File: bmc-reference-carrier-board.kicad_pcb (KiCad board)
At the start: 8 copper layers, 120.4 x 90 mm, 40 parts, among them J1 PCB-Edge_DC-SCM-2.1_2x84_Rev-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, J2 USB-C_GCT_USB4105-GF-A, J3 USB-C_GCT_USB4105-GF-A, J4 USB-C_GCT_USB4105-GF-A, J5 L834-1G1T-S7, J6 DisplayPort-Mini_TE_2129320-3, J7 Bus_M.2_1-2199230-6, J8 TFM-107-01-X-D-RE1-WT, Q1 BSS84AKW, U1 USB2514B-I_M2, U14 OSM-L_Carrier-side, U15 CBTL02043ABQ, U2 RTL8211FS-CG, U3 SDINBDG4-8G, U5 FT4232H_VQFN, U6 NCP718BSN330T1G, U7 AP22615A_TSOT26, U8 AP22615A_TSOT26, Y1 Resonator_12MHz_ABM8G

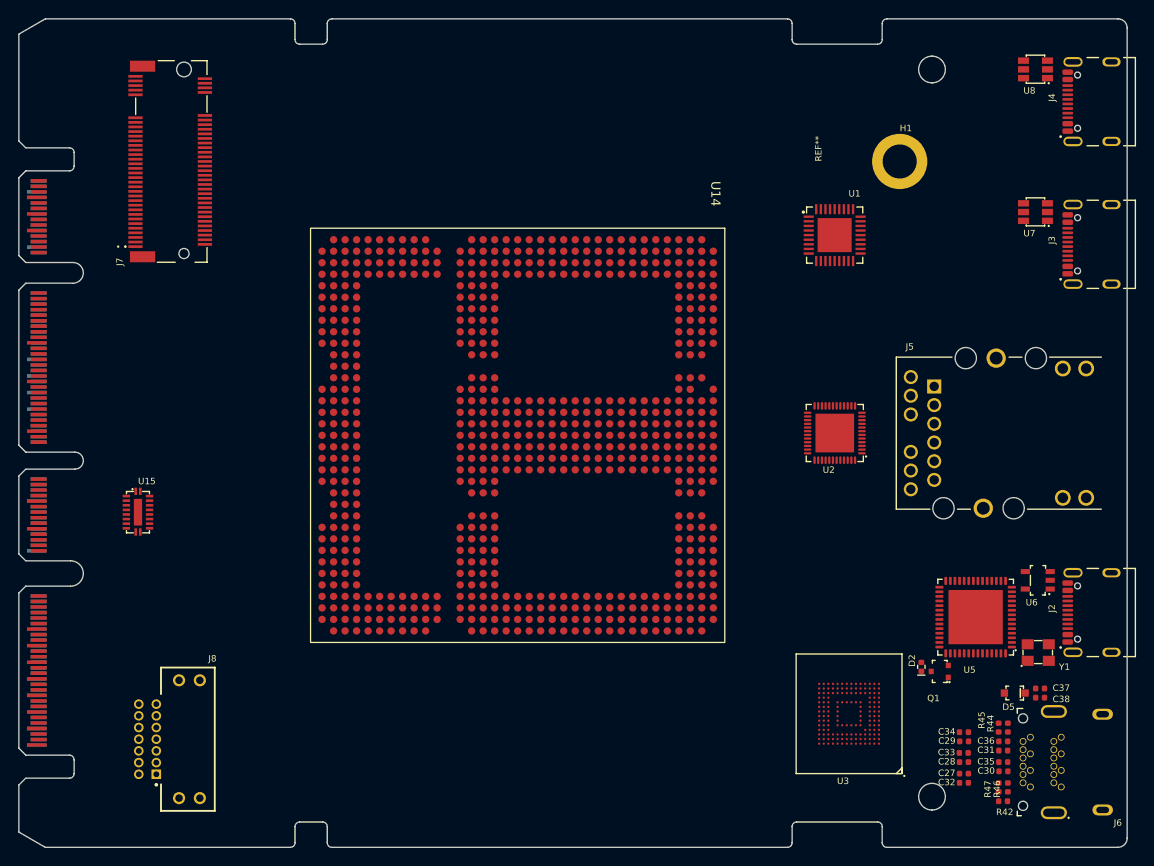
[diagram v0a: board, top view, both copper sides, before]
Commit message: [#82190] Update PCB from schematic
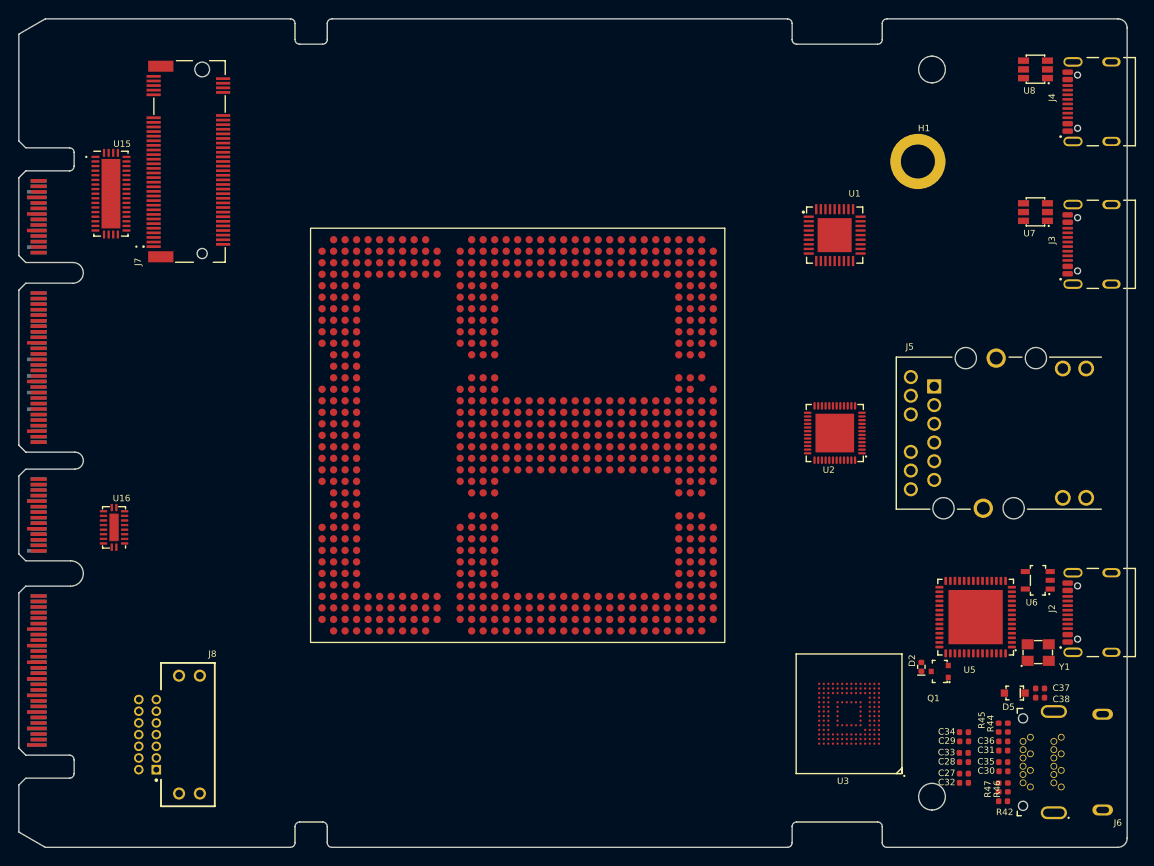
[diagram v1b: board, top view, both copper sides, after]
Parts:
- removed REF**: Mech_M2_2280_H2.5mm, antmicro-footprints:Mech_M2_2280_H2.5mm
- added U16: TMUXHS4212IRKSR, antmicro-footprints:VQFN-20_1EP_4.5x2.5mm_P0.5mm, F.Cu at (105.4, 96.2)
- U15: value CBTL02043ABQ -> TMUXHS4412RUAR; footprint antmicro-footprints:DHVQFN-20-1EP_2.5x4.5_P0.5mm -> antmicro-footprints:WQFN-42-1EP_3.5x9mm_P0.5mm
- moved U15 34.7 mm to (105.1, 60.0)
- moved H1 1.98 mm to (192.7, 56.5)
- moved J7 1.98 mm to (113.5, 56.5)
- moved J8 0.50 mm to (109.0, 118.8)
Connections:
- net /OSM L/OSM_PCIe_A.RX+ renamed /DC-SCM 2.1 connector/DC-SCM_PCIe0.RX2-
- net /OSM L/OSM_PCIe_A.RX- renamed /DC-SCM 2.1 connector/DC-SCM_PCIe0.RX2+
- net /OSM L/OSM_USB_C_SS.RX- renamed /PCIe - SGMII Mux/~{PCIE_USB_MUX_OE}
- net /OSM L/OSM_USB_C_SS.TX+ renamed /PCIe - SGMII Mux/PCIE_USB_MUX_SEL
- net /PCIe - USB Mux/PCIe/USB.RX+ renamed /DC-SCM 2.1 connector/DC-SCM_PCIe0.TX1+
- net /PCIe - USB Mux/PCIe/USB.RX- renamed /DC-SCM 2.1 connector/DC-SCM_PCIe0.TX1-
- net /PCIe - USB Mux/PCIe/USB.TX+ renamed /DC-SCM 2.1 connector/DC-SCM_PCIe0.RX1+
- net /PCIe - USB Mux/PCIe/USB.TX- renamed /DC-SCM 2.1 connector/DC-SCM_PCIe0.RX1-
- J7 pad 11: unconnected-(J7-PET3_N-Pad11) -> /DC-SCM 2.1 connector/DC-SCM_PCIe0.TX3-
- J7 pad 13: unconnected-(J7-PET3_P-Pad13) -> /DC-SCM 2.1 connector/DC-SCM_PCIe0.TX3+
- J7 pad 17: unconnected-(J7-PER2_N-Pad17) -> /PCIe - SGMII Mux/PCIE_x4.RX2-
- J7 pad 19: unconnected-(J7-PER2_P-Pad19) -> /PCIe - SGMII Mux/PCIE_x4.RX2+
- J7 pad 23: unconnected-(J7-PET2_N-Pad23) -> /PCIe - SGMII Mux/PCIE_x4.TX2-
- J7 pad 25: unconnected-(J7-PET2_P-Pad25) -> /PCIe - SGMII Mux/PCIE_x4.TX2+
- J7 pad 29: unconnected-(J7-PER1_N-Pad29) -> /PCIe - SGMII Mux/PCIE_x4.RX1-
- J7 pad 31: unconnected-(J7-PER1_P-Pad31) -> /PCIe - SGMII Mux/PCIE_x4.RX1+
- J7 pad 35: unconnected-(J7-PET1_N-Pad35) -> /PCIe - SGMII Mux/PCIE_x4.TX1-
- J7 pad 37: unconnected-(J7-PET1_P-Pad37) -> /PCIe - SGMII Mux/PCIE_x4.TX1+
- J7 pad 41: unconnected-(J7-PER0_N-Pad41) -> /DC-SCM 2.1 connector/DC-SCM_PCIe0.RX0-
- J7 pad 43: unconnected-(J7-PER0_P-Pad43) -> /DC-SCM 2.1 connector/DC-SCM_PCIe0.RX0+
- J7 pad 47: unconnected-(J7-PET0_N-Pad47) -> /DC-SCM 2.1 connector/DC-SCM_PCIe0.TX0-
- J7 pad 49: unconnected-(J7-PET0_P-Pad49) -> /DC-SCM 2.1 connector/DC-SCM_PCIe0.TX0+
- J7 pad 5: unconnected-(J7-PER3_N-Pad5) -> /DC-SCM 2.1 connector/DC-SCM_PCIe0.RX3-
- J7 pad 7: unconnected-(J7-PER3_P-Pad7) -> /DC-SCM 2.1 connector/DC-SCM_PCIe0.RX3+
- U15 pad 1: +3V3 -> unconnected-(U15-NC-Pad1)
- U15 pad 10: +3V3 -> /DC-SCM 2.1 connector/DC-SCM_PCIe0.TX2+
- U15 pad 11: GND -> /DC-SCM 2.1 connector/DC-SCM_PCIe0.TX2-
- U15 pad 12: /OSM L/OSM_PCIe_A.TX- -> unconnected-(U15-NC-Pad12)
- U15 pad 13: /OSM L/OSM_PCIe_A.TX+ -> /PCIe - SGMII Mux/VCC
- U15 pad 16: /OSM L/OSM_USB_C_SS.TX- -> GND
- U15 pad 19: /OSM L/OSM_USB_C_SS.RX+ -> unconnected-(U15-NC-Pad19)
- U15 pad 2: GND -> unconnected-(U15-NC-Pad2)
- U15 pad 20: GND -> unconnected-(U15-NC-Pad20)
- U15 pad 5: GND -> /PCIe - SGMII Mux/VCC
- U15 pad 6: +3V3 -> GND
- U15 pad 9: /PCIe - USB Mux/pcie_usb_mux_sel -> GND

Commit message: [#82190] Add logotype
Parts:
- added REF**: LOGO, antmicro-footprints:nxp_logo, F.Cu at (160.2, 47.6)
- added REF**: OSHW-Logo_5.7x6mm_Copper, antmicro-footprints:OSHW-Logo_5.7x6mm_Copper, F.Cu at (155.4, 125.7)
- added REF**: LOGO, antmicro-footprints:lattice_logo, F.Cu at (138.3, 48.3)
- added REF**: antmicro-logo_scaled_15mm, antmicro-footprints:antmicro-logo_scaled_15mm, F.Cu at (169.0, 125.9)
- added REF**: OSHW-Logo_5.7x6mm_Mask, antmicro-footprints:OSHW-Logo_5.7x6mm_Mask, F.Cu at (155.4, 125.7)
- moved U3 5.42 mm to (183.2, 111.5)

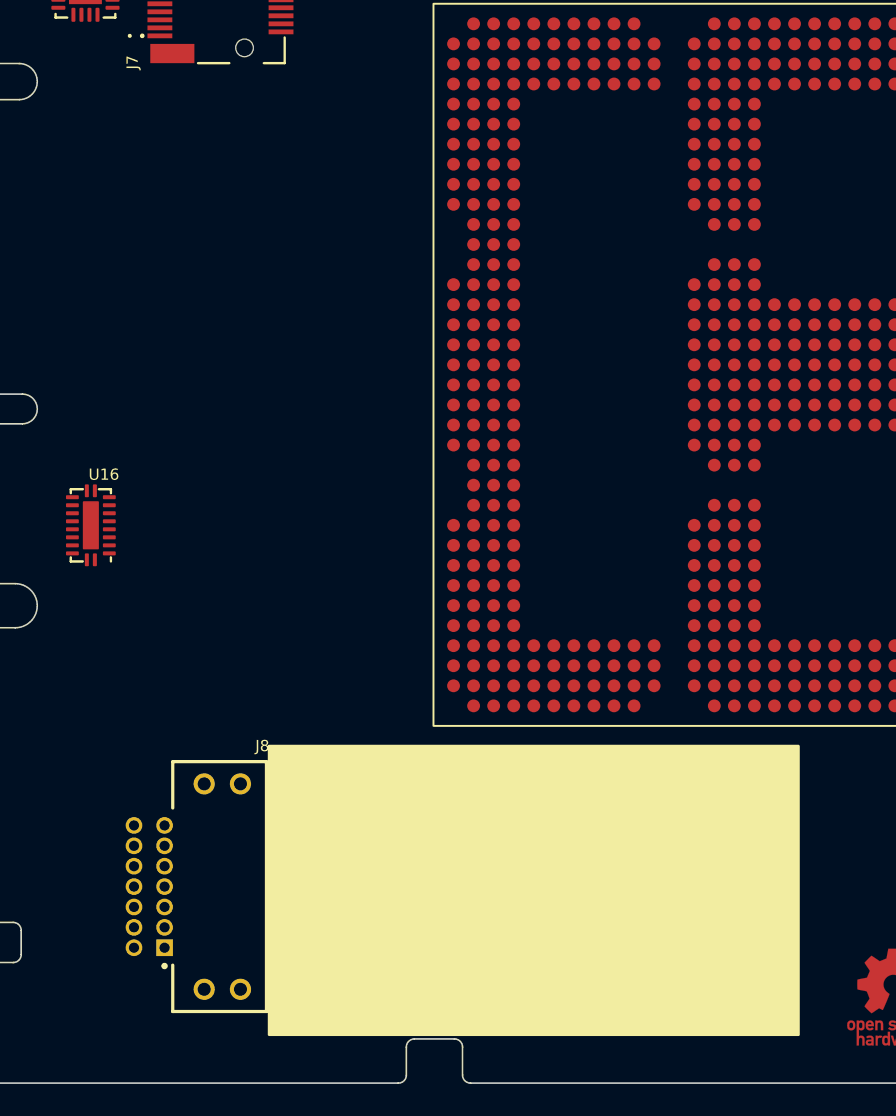
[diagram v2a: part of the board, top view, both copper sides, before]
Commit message: [#82190] Update PCB from schematic
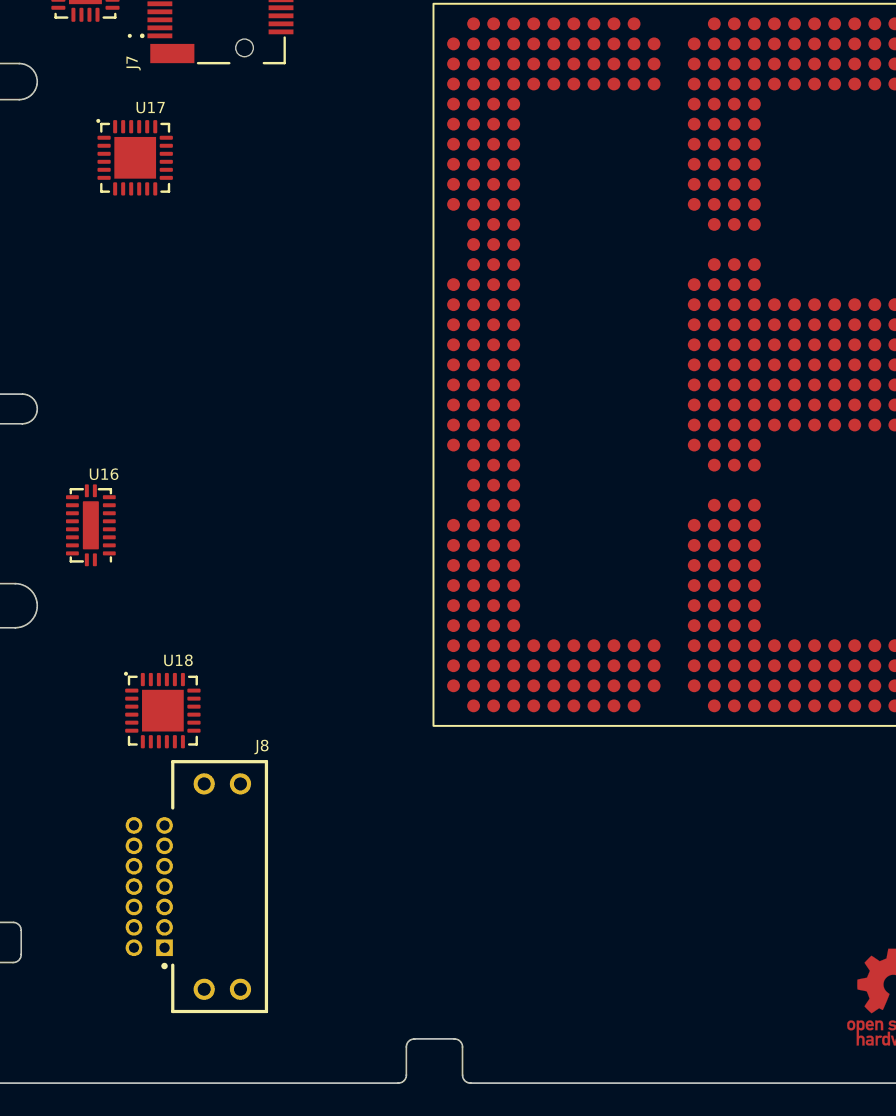
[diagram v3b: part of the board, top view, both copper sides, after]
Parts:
- added U17: TS3A27518E_QFN, antmicro-footprints:QFN-24-1EP_4x4mm_P0.5mm_EP2.6x2.6mm, F.Cu at (108.2, 73.3)
- added U18: TS3A27518E_QFN, antmicro-footprints:QFN-24-1EP_4x4mm_P0.5mm_EP2.6x2.6mm, F.Cu at (109.9, 107.8)
